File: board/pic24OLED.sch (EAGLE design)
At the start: 10 parts, among them U1 PIC24FJ64GA002T-I/ML

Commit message: Finished up first board draft completely.
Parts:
- added 10UF, 10UFPWR: THCAP, pic24fj64ga002:THCAP
- added THROBLED: THLED, pic24fj64ga002:THLED
- renumbered U$1 to 10KRES
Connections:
- new net N$22: 10UF.P$1, U1.VCAP/VDDCORE
- new net N$23: 10UF.P$2, U1.DISVREG
- net GND: now also 10UFPWR.P$2
- net N$14: now also THROBLED.GND
- net VDD: now also 10UFPWR.P$1, THROBLED.PWR, U1.VSS_2

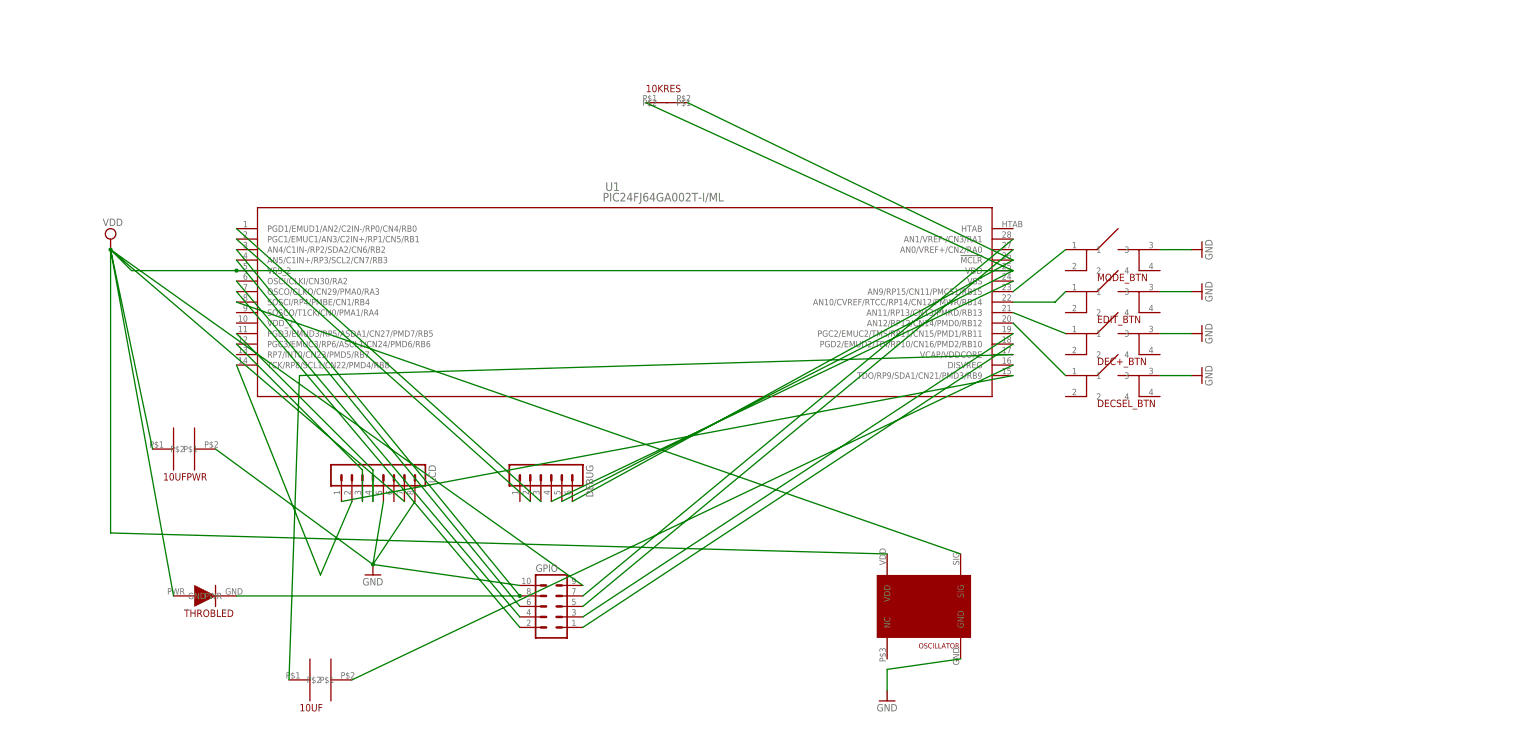
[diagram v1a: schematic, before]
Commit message: Board design v1.1
Used PIC layout I can actually solder. Moved some things around for easier access and made holes bigger.
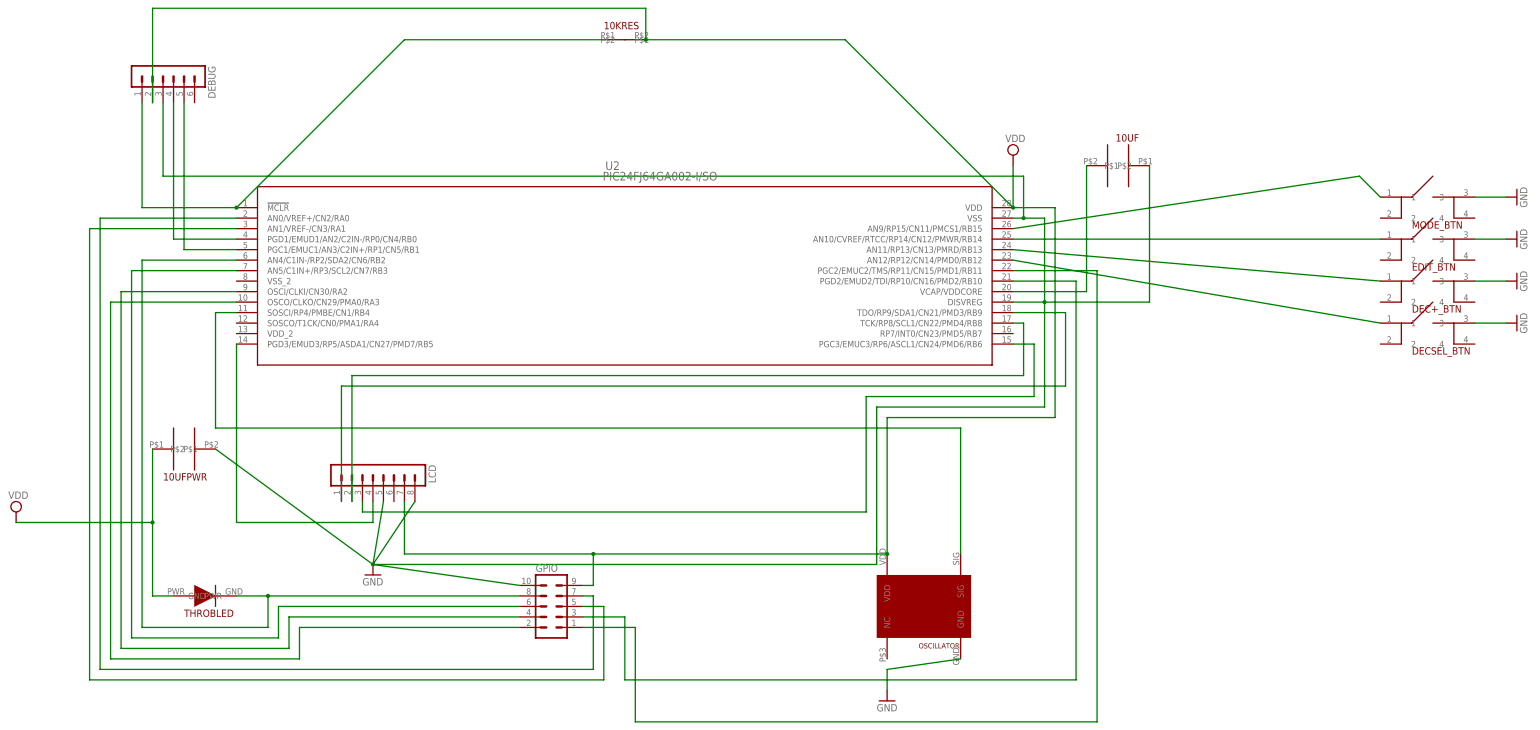
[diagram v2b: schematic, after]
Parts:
- removed U1: PIC24FJ64GA002T-I/ML, pic24fj64ga002:PIC24FJ64GA002T-I/ML
- added U2: PIC24FJ64GA002-I/SO, pic24fj64ga002:PIC24FJ64GA002-I/SO
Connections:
- removed net N$22: 10UF.P$1, U1.VCAP/VDDCORE
- removed net N$23: 10UF.P$2, U1.DISVREG
- net GND: now also 10UF.P$1, DEBUG.3, U2.DISVREG, U2.VSS
- net N$1: now also 10KRES.P$1, DEBUG.1, U2.!MCLR; no longer MODE_BTN.1, U1.AN9/RP15/CN11/PMCS1/RB15
- net N$10: now also LCD.1, U2.TDO/RP9/SDA1/CN21/PMD3/RB9; no longer LCD.2, U1.TCK/RP8/SCL1/CN22/PMD4/RB8
- net N$11: now also 10UF.P$2, U2.VCAP/VDDCORE; no longer LCD.3, U1.PGC3/EMUC3/RP6/ASCL1/CN24/PMD6/RB6
- net N$12: now also GPIO.6, U2.AN5/C1IN+/RP3/SCL2/CN7/RB3; no longer LCD.4, U1.PGD3/EMUD3/RP5/ASDA1/CN27/PMD7/RB5
- net N$13: now also OSCILLATOR.SIG, U2.SOSCI/RP4/PMBE/CN1/RB4; no longer 10KRES.P$2, DEBUG.6, U1.!MCLR
- net N$14: now also U2.AN4/C1IN-/RP2/SDA2/CN6/RB2; no longer U1.AN4/C1IN-/RP2/SDA2/CN6/RB2
- net N$15: now also DEBUG.4, U2.PGD1/EMUD1/AN2/C2IN-/RP0/CN4/RB0; no longer GPIO.6, U1.AN5/C1IN+/RP3/SCL2/CN7/RB3
- net N$16: now also DEBUG.5, U2.PGC1/EMUC1/AN3/C2IN+/RP1/CN5/RB1; no longer GPIO.4, U1.OSCI/CLKI/CN30/RA2
- net N$17: now also U2.OSCO/CLKO/CN29/PMA0/RA3; no longer U1.OSCO/CLKO/CN29/PMA0/RA3
- net N$18: now also U2.AN0/VREF+/CN2/RA0; no longer U1.AN1/VREF-/CN3/RA1
- net N$19: now also U2.AN1/VREF-/CN3/RA1; no longer U1.AN0/VREF+/CN2/RA0
- net N$2: now also GPIO.4, U2.OSCI/CLKI/CN30/RA2; no longer DEBUG.2, U1.PGC1/EMUC1/AN3/C2IN+/RP1/CN5/RB1
- net N$20: now also U2.PGD2/EMUD2/TDI/RP10/CN16/PMD2/RB10; no longer U1.PGC2/EMUC2/TMS/RP11/CN15/PMD1/RB11
- net N$21: now also U2.PGC2/EMUC2/TMS/RP11/CN15/PMD1/RB11; no longer U1.PGD2/EMUD2/TDI/RP10/CN16/PMD2/RB10
- net N$3: now also MODE_BTN.1, U2.AN9/RP15/CN11/PMCS1/RB15; no longer EDIT_BTN.1, U1.AN10/CVREF/RTCC/RP14/CN12/PMWR/RB14
- net N$4: now also EDIT_BTN.1, U2.AN10/CVREF/RTCC/RP14/CN12/PMWR/RB14; no longer DEC+_BTN.1, U1.AN11/RP13/CN13/PMRD/RB13
- net N$5: now also DEC+_BTN.1, U2.AN11/RP13/CN13/PMRD/RB13; no longer DECSEL_BTN.1, U1.AN12/RP12/CN14/PMD0/RB12
- net N$6: now also DECSEL_BTN.1, U2.AN12/RP12/CN14/PMD0/RB12; no longer DEBUG.3, U1.PGD1/EMUD1/AN2/C2IN-/RP0/CN4/RB0
- net N$7: now also LCD.4, U2.PGD3/EMUD3/RP5/ASDA1/CN27/PMD7/RB5; no longer OSCILLATOR.SIG, U1.SOSCI/RP4/PMBE/CN1/RB4
- net N$8: now also LCD.3, U2.PGC3/EMUC3/RP6/ASCL1/CN24/PMD6/RB6; no longer DEBUG.4, U1.VSS
- net N$9: now also LCD.2, U2.TCK/RP8/SCL1/CN22/PMD4/RB8; no longer LCD.1, U1.TDO/RP9/SDA1/CN21/PMD3/RB9
- net VDD: now also 10KRES.P$2, DEBUG.2, U2.VDD; no longer 10KRES.P$1, DEBUG.5, U1.VDD, U1.VSS_2
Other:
- moved on the sheet: 10KRES, 10UF, DEBUG, DEC+_BTN, DECSEL_BTN, EDIT_BTN, MODE_BTN
